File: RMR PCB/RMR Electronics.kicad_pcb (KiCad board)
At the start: 2 copper layers, 3.5 x 7 mm, 19 parts, among them J1 Arduino Power, J2 RPI Power, J3 Mast Servo, J4 RMotor, J5 LMotor, J6 Conn_01x01_Male, J7 LMotor Control, J8 RMotor Control, J9 PJ-037A, U1 AP2204R-5.0, U2 AP2204R-5.0

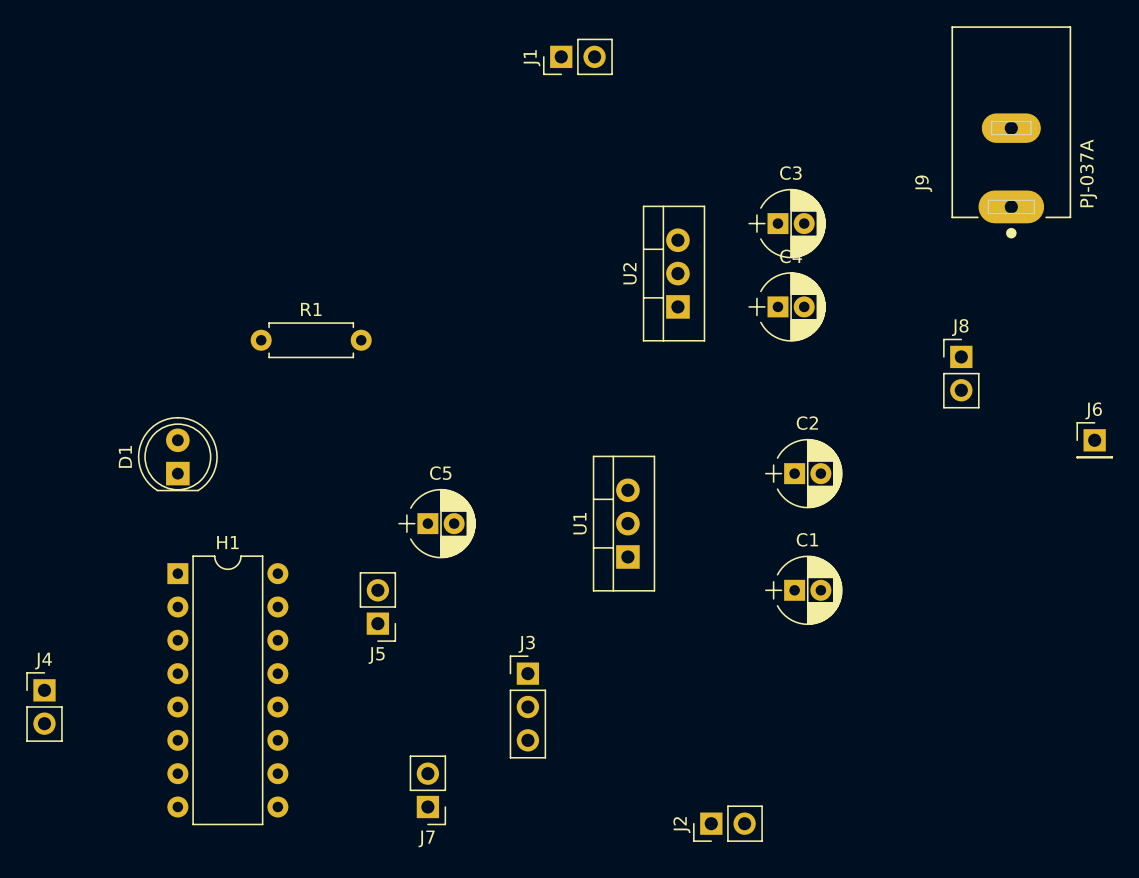
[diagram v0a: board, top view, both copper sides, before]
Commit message: reduced  PCB size drastically, outstanding GND copper pour issue
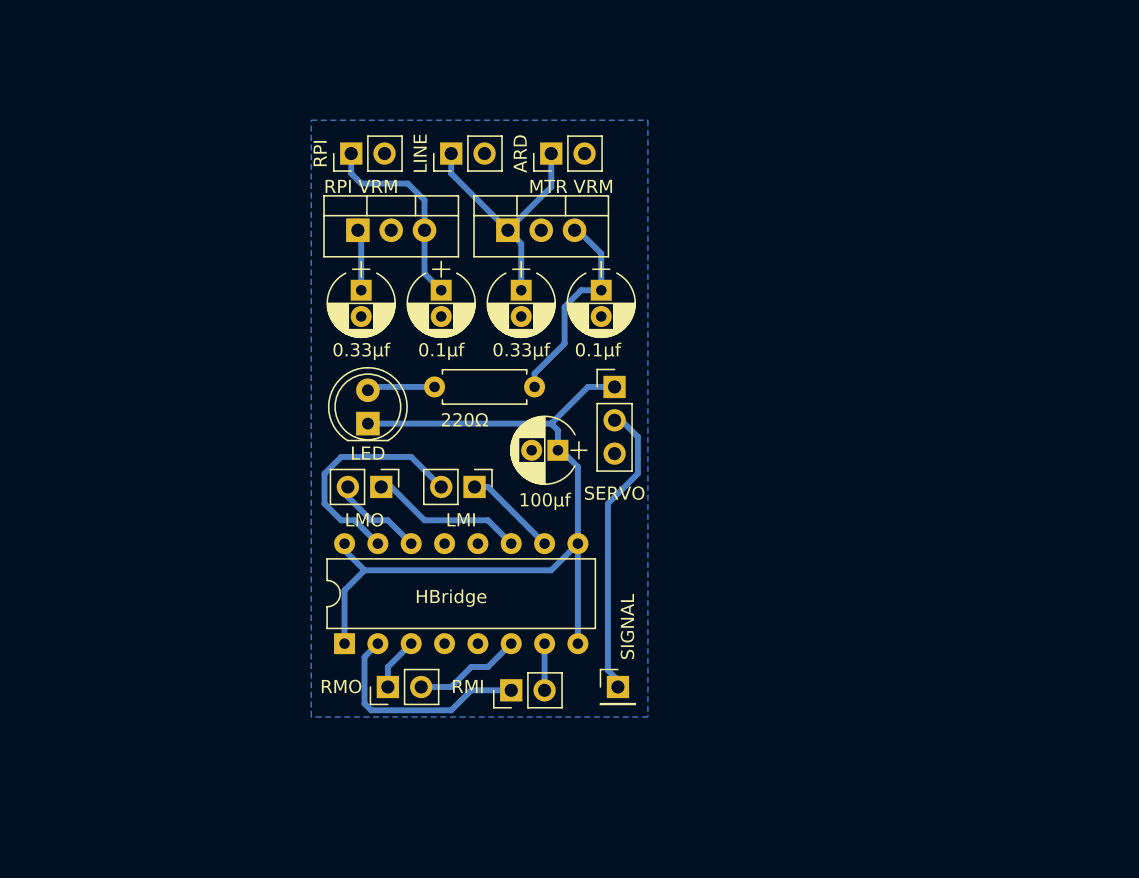
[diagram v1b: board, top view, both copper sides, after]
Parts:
- removed J9: PJ-037A, PJ-037A:CUI_PJ-037A
- added LINE: Power In, Pin_Headers:Pin_Header_Straight_1x02_Pitch2.54mm, F.Cu at (132.6, 83.6)
- MTR VRM: renamed from U2
- RPI VRM: renamed from U1
- moved RPI 58.0 mm to (125.0, 83.6)
- moved RMI 42.7 mm to (137.2, 124.5), turned to 90 degrees
- moved SIGNAL 40.9 mm to (145.3, 124.2)
- moved 0.33μf 40.2 mm to (125.7, 94.0), turned to 270 degrees
- moved RPI VRM 32.3 mm to (125.5, 89.4), turned to 0 degrees
- moved 0.1μf 30.3 mm to (131.8, 94.0), turned to 270 degrees
- moved RMO 26.2 mm to (127.8, 124.2), turned to 90 degrees
- moved LMI 24.6 mm to (134.4, 109.0), turned to 270 degrees
- moved SERVO 22.8 mm to (145.0, 101.3)
- moved 0.33μf 20.2 mm to (137.9, 94.0), turned to 270 degrees
- moved LED 15.0 mm to (126.2, 104.1)
- moved MTR VRM 14.2 mm to (136.9, 89.4), turned to 0 degrees
- moved HBridge 13.8 mm to (124.5, 120.9), turned to 90 degrees
- moved 220Ω 13.7 mm to (131.3, 101.3)
- moved 0.1μf 13.5 mm to (144.0, 94.0), turned to 270 degrees
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- renumbered C2 to 0.1μf, C4 to 0.1μf, C1 to 0.33μf, C3 to 0.33μf, C5 to 100μf, R1 to 220Ω, J1 to ARD, H1 to HBridge, D1 to LED, J7 to LMI, J5 to LMO, J8 to RMI, J4 to RMO, J2 to RPI, J3 to SERVO, J6 to SIGNAL
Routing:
- net Net-(C5-Pad1): track 0.00 -> 63.7 mm
- net Net-(C1-Pad1): track 0.00 -> 24.5 mm
- net Net-(J3-Pad2): track 0.00 -> 22.6 mm
- net Net-(H1-Pad15): track 0.00 -> 18.0 mm
- net Net-(H1-Pad2): track 0.00 -> 17.0 mm
- net Net-(C4-Pad1): track 0.00 -> 15.9 mm
- net Net-(C2-Pad1): track 0.00 -> 15.3 mm
- net Net-(H1-Pad11): track 0.00 -> 11.7 mm
- net Net-(H1-Pad6): track 0.00 -> 8.48 mm
- net Net-(H1-Pad10): track 0.00 -> 7.12 mm
- net Net-(H1-Pad14): track 0.00 -> 7.06 mm
- net Net-(D1-Pad2): track 0.00 -> 5.19 mm
- net Net-(H1-Pad3): track 0.00 -> 4.04 mm
- net Net-(H1-Pad7): track 0.00 -> 3.56 mm
- added copper zone on B.Cu, net GND
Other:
- board outline removed

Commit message: cleaned up
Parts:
- HBridge (machine broke): renamed from HBridge
- moved SERVO 3.06 mm to (145.3, 104.4)
- moved 100μf 2.05 mm to (138.7, 106.4), turned to 0 degrees
- moved RMI 0.25 mm to (137.2, 124.2)
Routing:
- net Net-(C1-Pad1): track 24.5 -> 42.6 mm
- net Net-(C5-Pad1): track 63.7 -> 67.0 mm
- net Net-(J3-Pad2): track 22.6 -> 20.3 mm
- net Net-(C2-Pad1): track 15.3 -> 14.1 mm
- net Net-(H1-Pad15): track 18.0 -> 18.9 mm
- net Net-(C4-Pad1): track 15.9 -> 15.1 mm
- net Net-(H1-Pad11): track 11.7 -> 12.5 mm
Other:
- board outline added: 26.7 x 46.5 mm
- board text added: "Designed in Oakville, Canada RMR V1"
- board text added: "RMR v1"

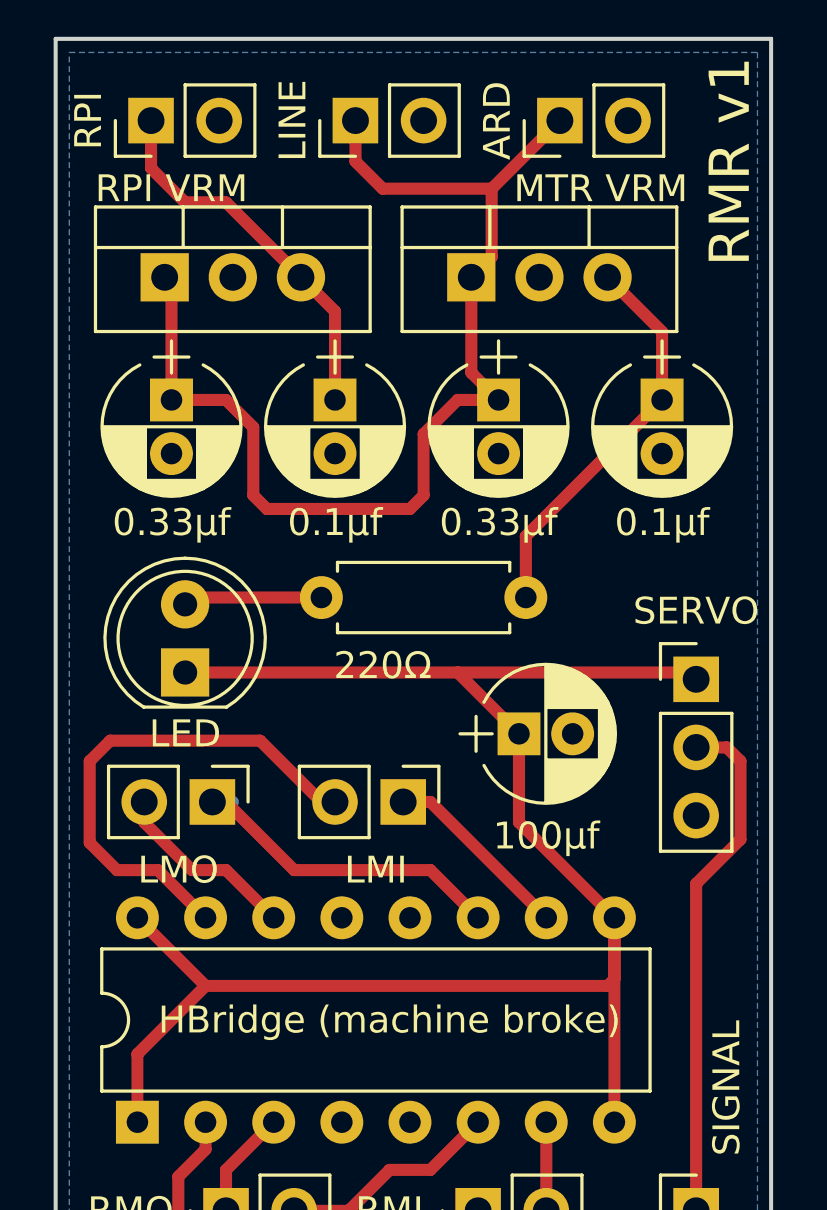
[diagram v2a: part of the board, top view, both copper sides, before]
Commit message: Fixed up an issue with the indicator LED
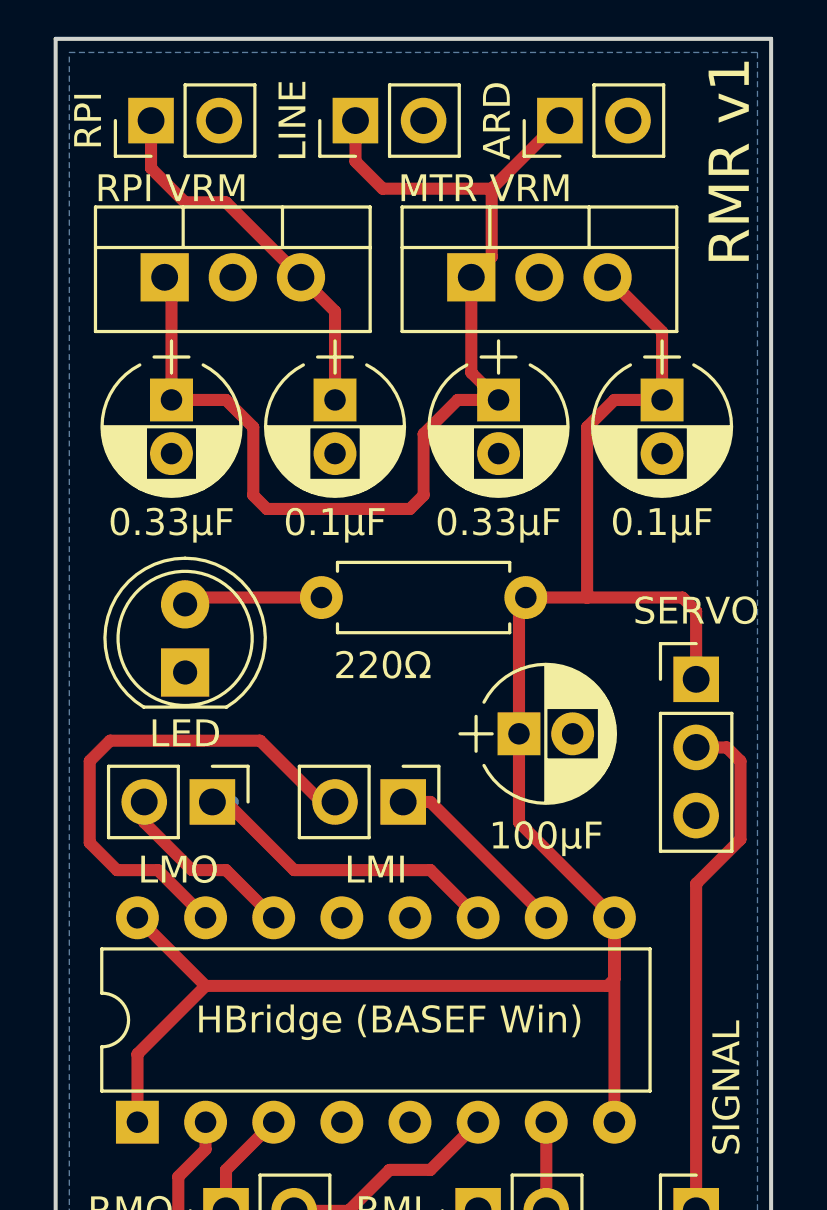
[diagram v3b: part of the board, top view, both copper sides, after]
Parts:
- HBridge (BASEF Win): renamed from HBridge (machine broke)
- RPI VRM: value AP2204R-5.0 -> RPI VRM
- SIGNAL: value Conn_01x01_Male -> SIGNAL
- renumbered 0.1μf to 0.1μF, 0.33μf to 0.33μF, 100μf to 100μF
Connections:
- 100μF pad 1: Net-(C5-Pad1) -> Net-(C4-Pad1)
- LED pad 1: Net-(C5-Pad1) -> GND
- SERVO pad 1: Net-(C5-Pad1) -> Net-(C4-Pad1)
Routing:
- net Net-(C5-Pad1): track 67.0 -> 40.8 mm
- net Net-(C4-Pad1): track 15.1 -> 33.7 mm

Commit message: Finalized logo and design
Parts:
- added G***: LOGO, mod:RMRlogo, B.Cu at (134.6, 88.9)
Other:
- board text added: "Designed in Oakville, Canada by Erik and Ethan"
- board text removed: "Designed in Oakville, Canada RMR V1"

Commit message: updates
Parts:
- moved G*** 0.25 mm to (134.6, 88.6)
